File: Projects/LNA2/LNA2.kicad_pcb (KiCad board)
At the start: 2 copper layers, 24.2 x 16.4 mm, 9 parts, among them J1 SMA-J-P-H-ST-EM1, J2 SMA-J-P-H-ST-EM1, U1 TRF37A73

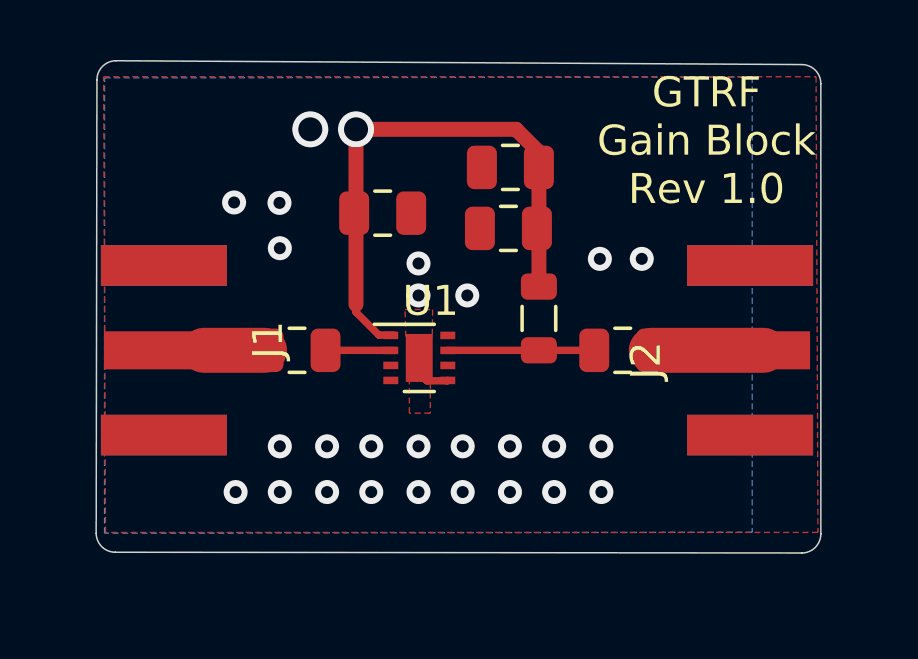
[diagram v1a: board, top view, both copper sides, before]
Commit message: fixed SMA connectors
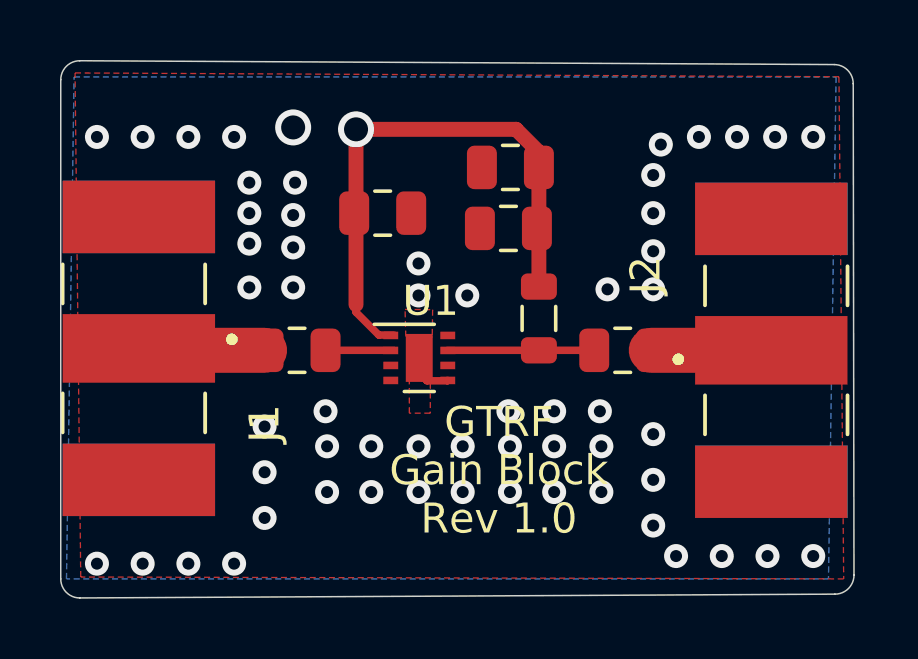
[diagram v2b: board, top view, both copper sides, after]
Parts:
- J1, J2: value SMA-J-P-H-ST-EM1 -> ECE4415PrefferedSMA; footprint SAMTEC_SMA-J-P-H-ST-EM1 -> AdditionalLibs:ECE4415PrefferedSMA
- moved J1 0.64 mm to (92.8, 80.2), turned to 90 degrees
- moved J2 0.51 mm to (113.9, 80.3), turned to 270 degrees
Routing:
- net GND: vias 26 -> 58
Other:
- board size 24.2 x 16.4 mm -> 26.4 x 17.9 mm

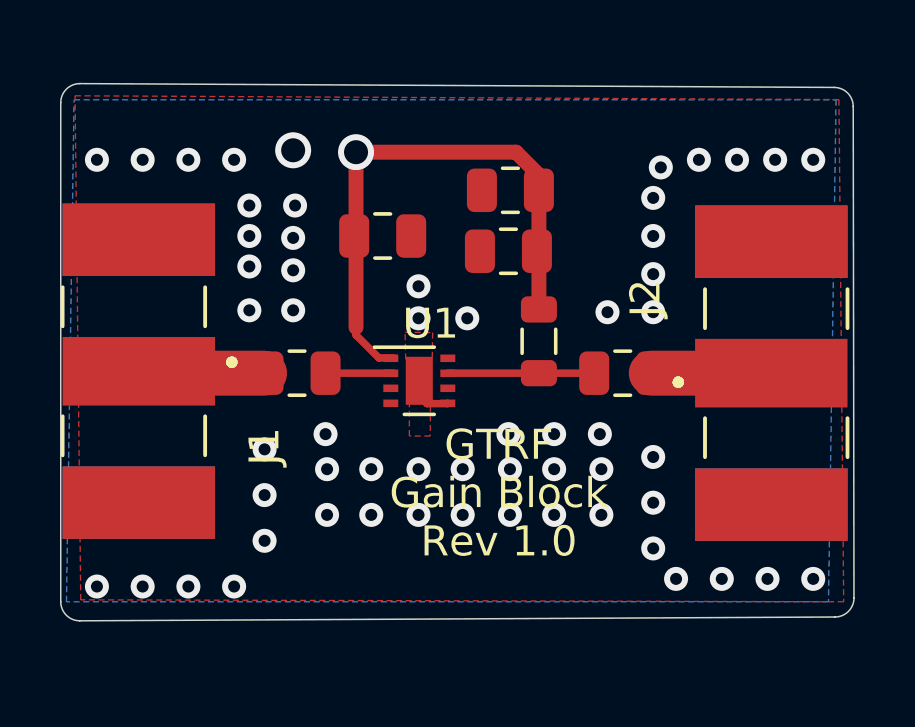
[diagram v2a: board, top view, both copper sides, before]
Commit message: added via stitching to the boards and changed to a barrel jack on the LNA
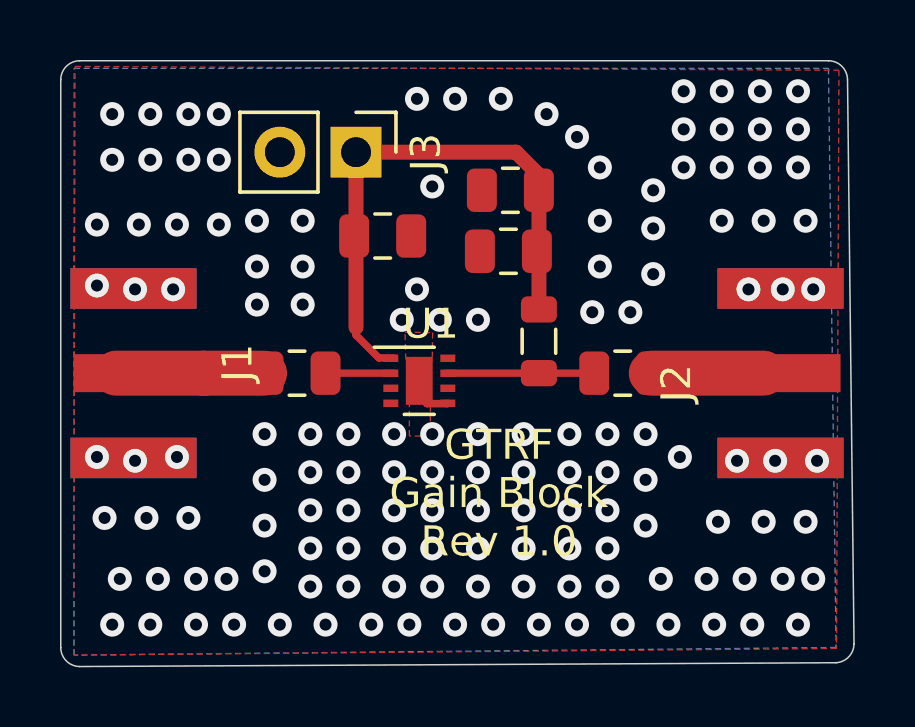
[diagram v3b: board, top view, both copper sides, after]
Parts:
- added J3: Conn_01x02, Connector_PinHeader_2.54mm:PinHeader_1x02_P2.54mm_Vertical, F.Cu at (100.1, 72.9)
- J1, J2: value ECE4415PrefferedSMA -> SMA-J-P-H-ST-EM1; footprint AdditionalLibs:ECE4415PrefferedSMA -> AdditionalLibs:SAMTEC_SMA-J-P-H-ST-EM1
- moved J2 0.51 mm to (114.4, 80.3), turned to 90 degrees
- moved J1 0.39 mm to (92.5, 80.3), turned to 270 degrees
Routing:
- net Net-(CC1-Pad2): track 2.03 -> 4.95 mm
- net VCC: vias 1 -> 0
- net GND: vias 58 -> 143
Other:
- board size 26.4 x 17.9 mm -> 26.4 x 20.2 mm

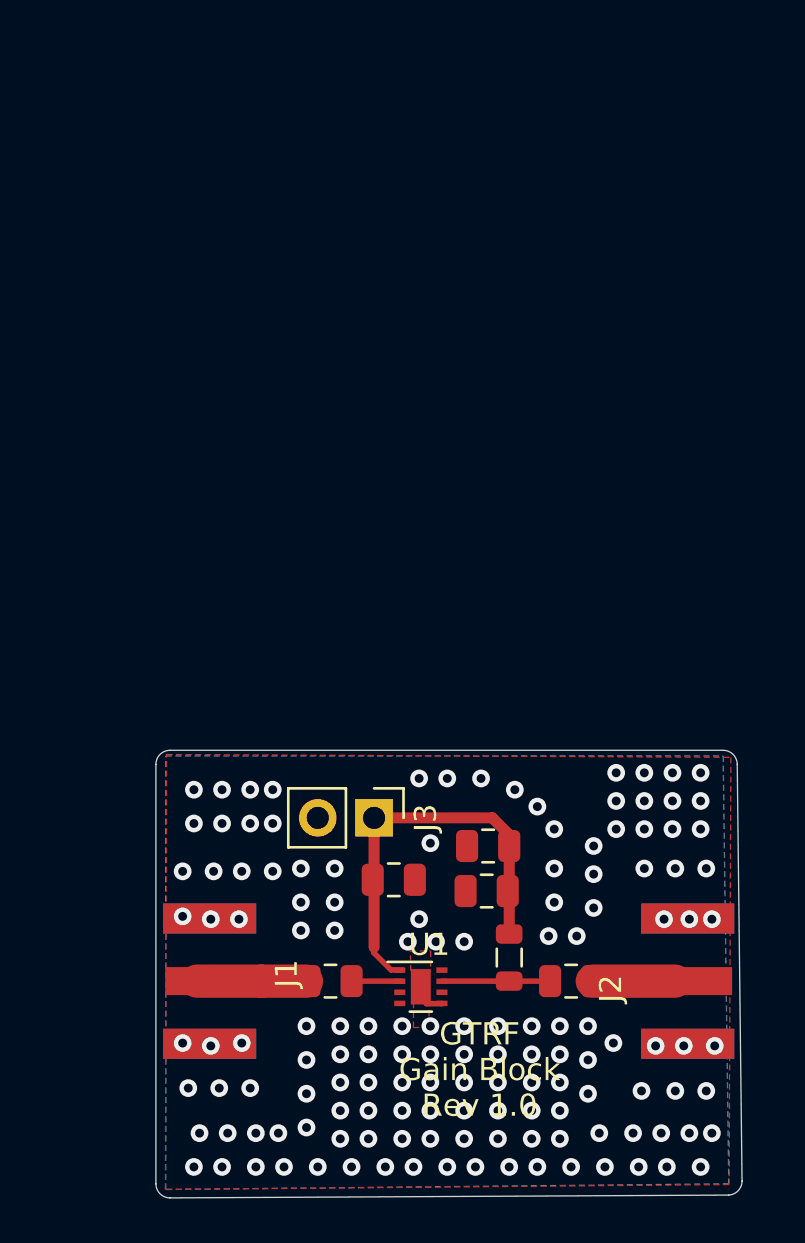
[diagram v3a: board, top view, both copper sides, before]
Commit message: added linear reg to the rf gain block
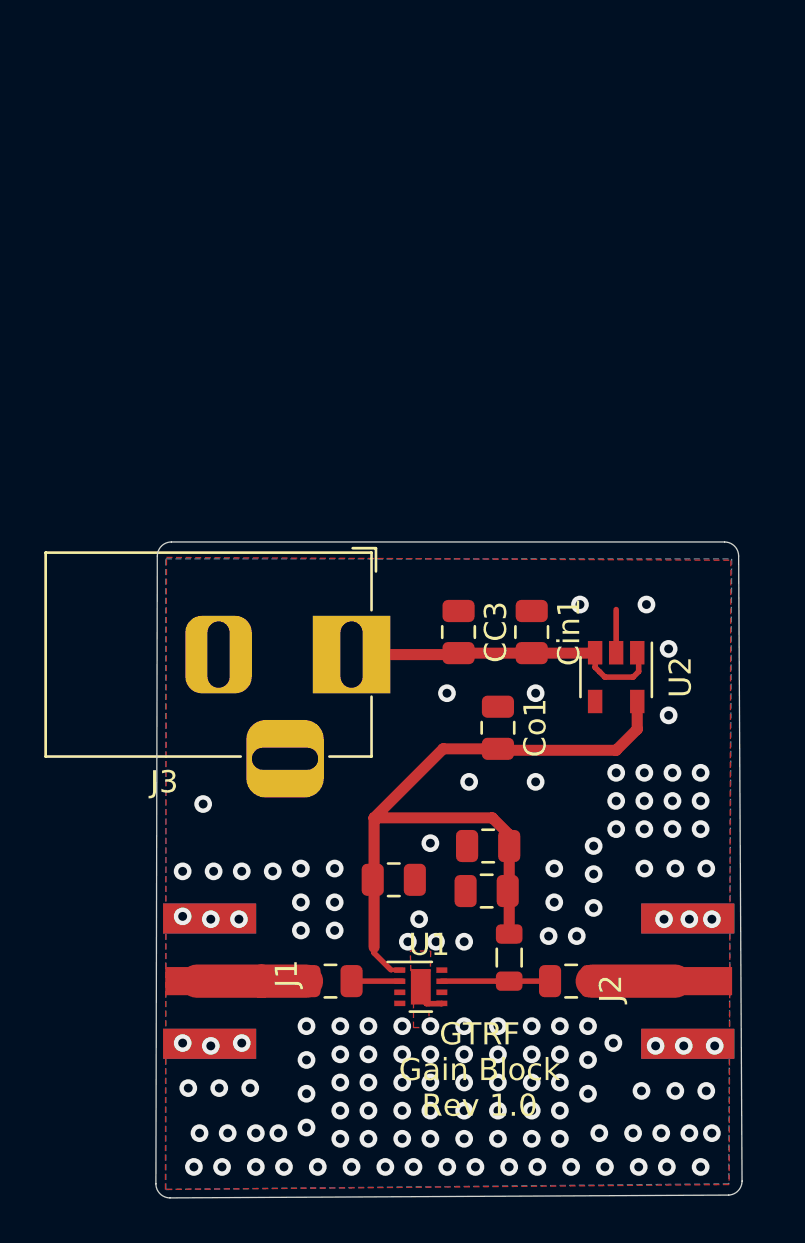
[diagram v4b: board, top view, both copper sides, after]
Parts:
- added CC3: 10u, Capacitor_SMD:C_0805_2012Metric, F.Cu at (103.9, 64.5)
- added Cin1: 1u, Capacitor_SMD:C_0805_2012Metric, F.Cu at (107.2, 64.5)
- added Co1: 1u, Capacitor_SMD:C_0805_2012Metric, F.Cu at (105.7, 68.8)
- added U2: TPS7A0533PDBV, Package_TO_SOT_SMD:SOT-23-5, F.Cu at (111.0, 66.5)
- J1, J2: footprint AdditionalLibs:SAMTEC_SMA-J-P-H-ST-EM1 -> SAMTEC_SMA-J-P-H-ST-EM1
- J3: value Conn_01x02 -> Barrel_Jack_MountingPin; footprint Connector_PinHeader_2.54mm:PinHeader_1x02_P2.54mm_Vertical -> Connector_BarrelJack:BarrelJack_Horizontal
- moved J3 7.44 mm to (99.1, 65.5), turned to 0 degrees
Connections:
- CDC1 pad 1: VCC -> Net-(CDC1-Pad1)
- CRF1 pad 1: VCC -> Net-(CDC1-Pad1)
- CRF2 pad 1: VCC -> Net-(CDC1-Pad1)
- LRF1 pad 1: VCC -> Net-(CDC1-Pad1)
- U1 pad 1: VCC -> Net-(CDC1-Pad1)
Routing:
- net Net-(CDC1-Pad1): track 0.00 -> 34.3 mm
- net VCC: track 19.0 -> 14.7 mm
- net GND: track 1.34 -> 3.28 mm, vias 143 -> 138
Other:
- board size 26.4 x 20.2 mm -> 26.4 x 29.6 mm

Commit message: Created a new file
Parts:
- CC3: footprint Capacitor_SMD:C_0805_2012Metric -> Capacitor_SMD:C_1206_3216Metric
- moved J3 13.3 mm to (98.2, 52.3), turned to 270 degrees
- moved U2 12.1 mm to (99.1, 64.8)
- moved Cin1 9.09 mm to (99.1, 60.5), turned to 180 degrees
- moved CC3 8.59 mm to (99.7, 57.0), turned to 180 degrees
- moved Co1 4.70 mm to (101.0, 69.0), turned to 180 degrees
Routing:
- net Net-(CDC1-Pad1): track 34.3 -> 26.1 mm
- net VCC: track 14.7 -> 15.4 mm
- net GND: track 3.28 -> 2.88 mm, vias 138 -> 215
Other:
- board size 26.4 x 29.6 mm -> 26.9 x 47.9 mm

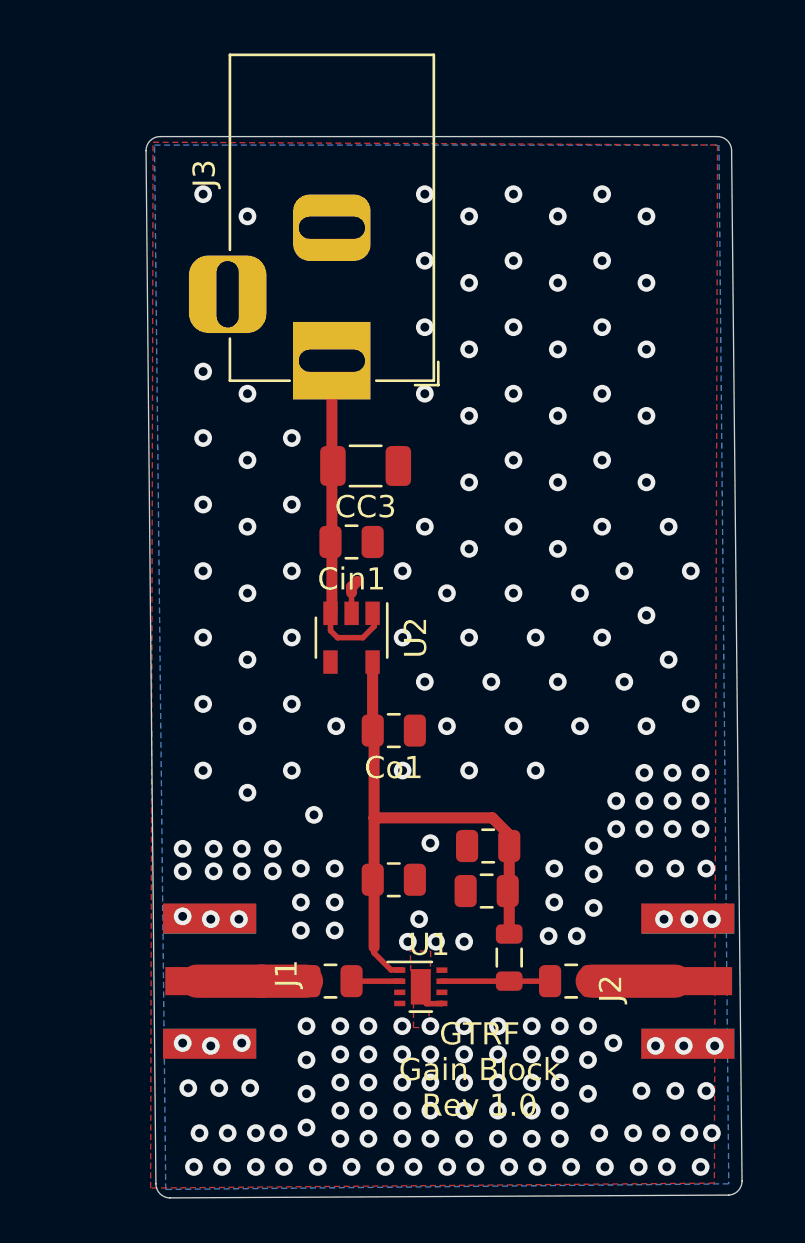
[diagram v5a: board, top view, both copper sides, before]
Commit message: added a demodulation board
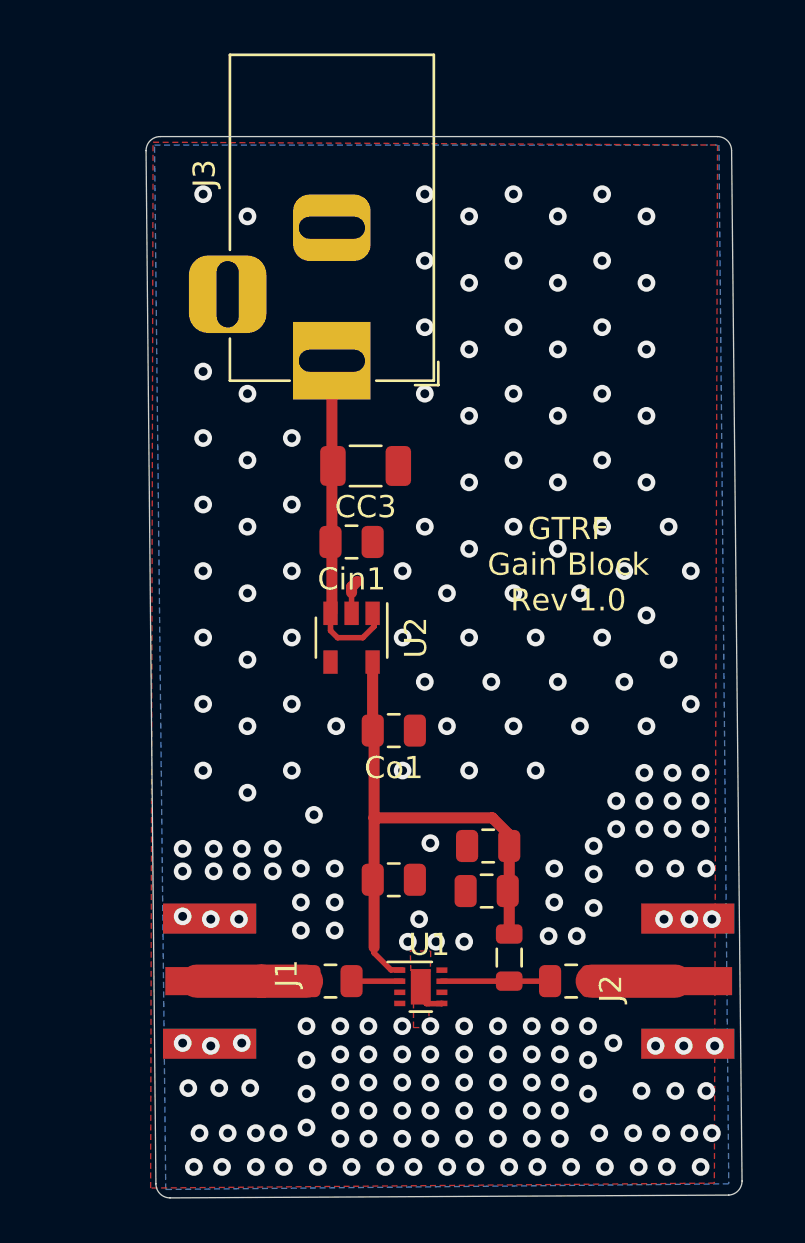
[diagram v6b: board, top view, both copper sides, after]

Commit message: post board review they are all ready to order
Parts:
- CC3: footprint Capacitor_SMD:C_1206_3216Metric -> Capacitor_Tantalum_SMD:CP_EIA-6032-28_Kemet-C
- J1, J2: footprint SAMTEC_SMA-J-P-H-ST-EM1 -> AdditionalLibs:SAMTEC_SMA-J-P-H-ST-EM1
- moved CRF2 1.14 mm to (105.2, 73.0)
- moved CC3 1.09 mm to (100.8, 56.9)
- moved CC2 0.89 mm to (109.9, 80.3)
- moved CC1 0.83 mm to (97.3, 80.3)
- moved CRF1 0.64 mm to (105.2, 75.6)
- moved J1 0.51 mm to (91.9, 80.3)
- moved J2 0.51 mm to (114.9, 80.3)
- moved J3 0.41 mm to (98.2, 51.9)
- moved Cin1 0.26 mm to (99.1, 60.7)
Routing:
- net GND: track 2.88 -> 5.10 mm, vias 215 -> 90
- net Net-(CC2-Pad1): track 3.75 -> 5.02 mm
- net Net-(CC2-Pad2): track 4.55 -> 5.57 mm
- net Net-(CDC1-Pad1): track 26.1 -> 27.0 mm
- net Net-(CC1-Pad1): track 2.29 -> 3.05 mm
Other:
- board size 26.9 x 47.9 mm -> 27.7 x 47.9 mm
